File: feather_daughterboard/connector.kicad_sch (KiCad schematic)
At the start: 1 part, among them J1 61300811121

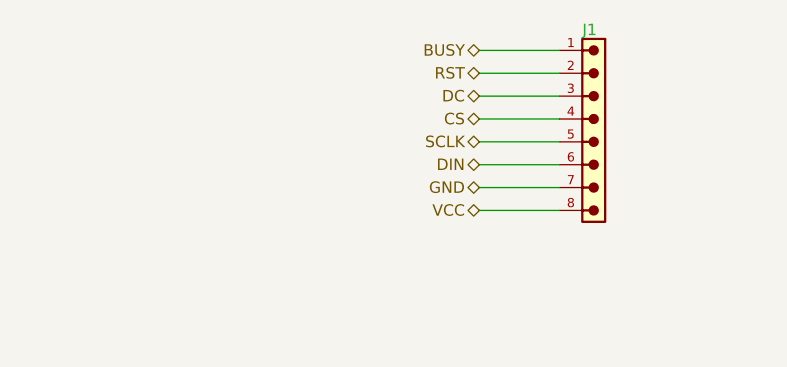
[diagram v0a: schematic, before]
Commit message: added daughter board
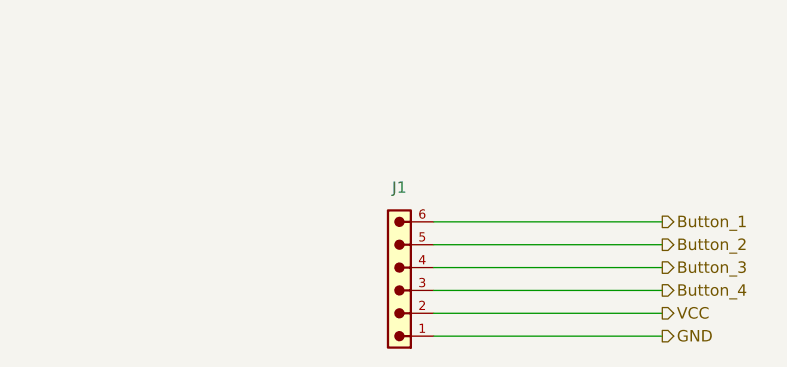
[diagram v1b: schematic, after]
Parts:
- removed J1: 61300811121, Custom footprints:61300811121, symbol 6130XX11121_61300811121:6130XX11121_61300811121
- added J1: 61900619521, Custom footprints:61900619521, symbol 61900619521:61900619521
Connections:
- net GND: now also J1.1
- net VCC: now also J1.2
- new net Button_1: J1.6
- new net Button_2: J1.5
- new net Button_3: J1.4
- new net Button_4: J1.3

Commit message: changed the connector on the daughter board
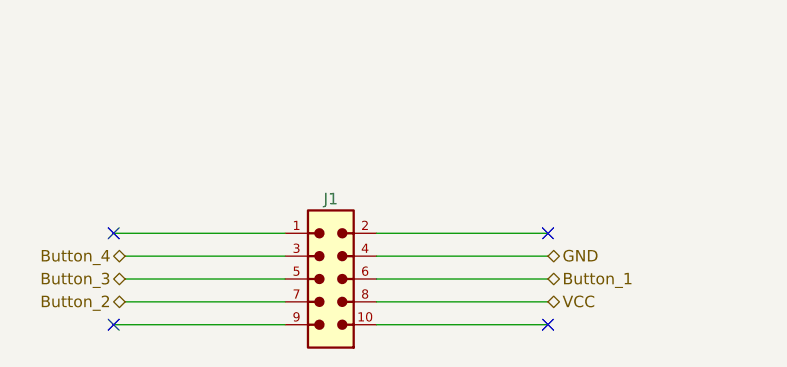
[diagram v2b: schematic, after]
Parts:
- removed J1: 61900619521, Custom footprints:61900619521, symbol 61900619521:61900619521
- added J1: 6250XX21721_62501021721, Custom footprints:62501021721, symbol 6250XX21721_62501021721:6250XX21721_62501021721
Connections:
- net Button_1: now also J1.6
- net Button_2: now also J1.7
- net Button_3: now also J1.5
- net Button_4: now also J1.3
- net GND: now also J1.4
- net VCC: now also J1.8
- no-connect marks 0 -> 4
